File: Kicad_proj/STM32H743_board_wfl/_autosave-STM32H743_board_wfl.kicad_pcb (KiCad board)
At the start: 4 copper layers, 38.5 x 38.5 mm, 64 parts, among them J1 GPS, J2 ESC, J3 UART, J4 Tag_Connect_6pin, U1 LT8609SEV#PBF, U2 AP7361C-33E, U3 STM32H743VITx, U4 W25Q512JVEIQ, U5 BMI088, Y1 8MHz Crystal

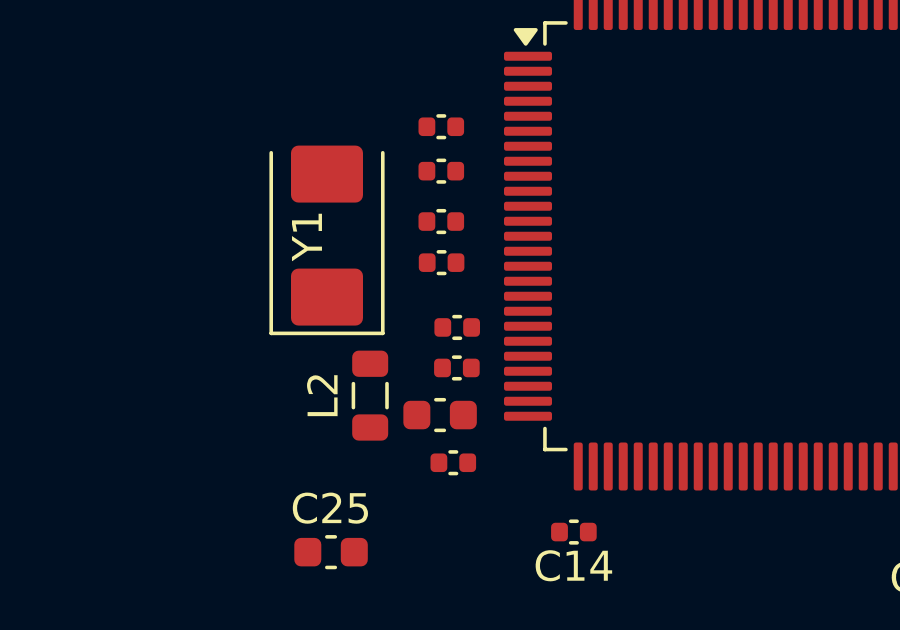
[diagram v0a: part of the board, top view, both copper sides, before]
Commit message: SCH v0.6 LT8609 NC -> GND
remove floats according to datasheet
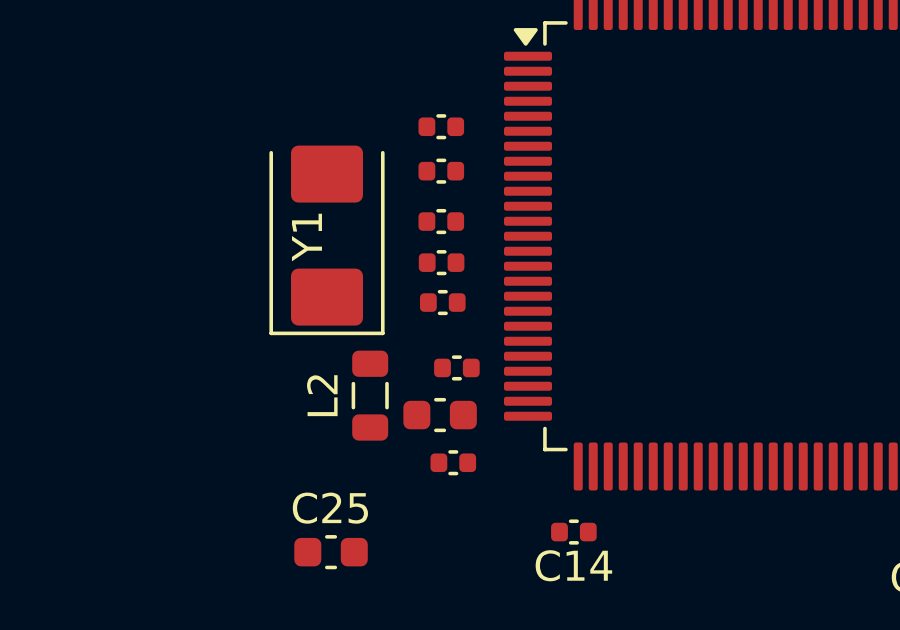
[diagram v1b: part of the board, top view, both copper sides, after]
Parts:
- moved C21 0.96 mm to (46.8, 173.3)
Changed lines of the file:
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@@
 	(footprint "Capacitor_SMD:C_0402_1005Metric"
 		(layer "F.Cu")
-		(at 47.27 174.1 180)
+		(at 46.79 173.27 180)
 		(descr "Capacitor SMD 0402 (1005 Metric), square (rectangular) end terminal, IPC-7351 nominal, (Body size source: IPC-SM-782 page 76, https://www.pcb-3d.com/wordpress/wp-content/uploads/ipc-sm-782a_amendment_1_and_2.pdf)")
 		(tags "capacitor")
